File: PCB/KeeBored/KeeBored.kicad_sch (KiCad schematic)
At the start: 114 parts, among them SW1 SW_Push, SW10 SW_Push, SW100 SW_Push, SW101 SW_Push, SW102 SW_Push, SW103 SW_Push, SW104 SW_Push, SW105 SW_Push, SW106 SW_Push, SW107 SW_Push, SW108 SW_Push, SW109 SW_Push, SW11 SW_Push, SW110 SW_Push, SW111 SW_Push, SW112 SW_Push, SW12 SW_Push, SW13 SW_Push, SW14 SW_Push, SW15 SW_Push, SW16 SW_Push, SW17 SW_Push, SW18 SW_Push, SW19 SW_Push, SW2 SW_Push, SW20 SW_Push, SW21 SW_Push, SW22 SW_Push, SW23 SW_Push, SW24 SW_Push, SW25 SW_Push, SW26 SW_Push, SW27 SW_Push, SW28 SW_Push, SW29 SW_Push, SW3 SW_Push, SW30 SW_Push, SW31 SW_Push, SW32 SW_Push, SW33 SW_Push, SW34 SW_Push, SW35 SW_Push, SW36 SW_Push, SW37 SW_Push, SW38 SW_Push, SW39 SW_Push, SW4 SW_Push, SW40 SW_Push, SW41 SW_Push, SW42 SW_Push, SW43 SW_Push, SW44 SW_Push, SW45 SW_Push, SW46 SW_Push, SW47 SW_Push, SW48 SW_Push, SW49 SW_Push, SW5 SW_Push, SW50 SW_Push, SW51 SW_Push, SW52 SW_Push, SW53 SW_Push, SW54 SW_Push, SW55 SW_Push, SW56 SW_Push, SW57 SW_Push, SW58 SW_Push, SW59 SW_Push, SW6 SW_Push, SW60 SW_Push, SW61 SW_Push, SW62 SW_Push, SW63 SW_Push, SW64 SW_Push, SW65 SW_Push, SW66 SW_Push, SW67 SW_Push, SW68 SW_Push, SW69 SW_Push, SW7 SW_Push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

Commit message: Create Key Matrix
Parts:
- removed SW110, SW111, SW112, SW12, SW83, SW97, SW98: SW_Push, symbol Switch:SW_Push
- added D10, D100, D101, D102, D103, D104, D105, D106, D107, D108, D109, D11, D12, D13, D14, D15, D16, D17, D18, D19, D2, D20, D21, D22, D23, D24, D25, D26, D27, D28, D29, D3, D30, D31, D32, D33, D34, D35, D36, D37, D38, D39, D4, D40, D41, D42, D43, D44, D45, D46, D47, D48, D49, D5, D50, D51, D52, D53, D54, D55, D56, D57, D58, D59, D6, D60, D61, D62, D63, D64, D65, D66, D67, D68, D69, D7, D70, D71, D72, D73, D74, D75, D76, D77, D78, D79, D8, D80, D81, D82, D84, D85, D86, D87, D88, D89, D9, D90, D91, D92, D93, D94, D95, D96, D99: 1N4148, Diode_THT:D_DO-35_SOD27_P7.62mm_Horizontal, symbol Diode:1N4148
- added J1: OLED, symbol Connector:Conn_01x04_Pin
- added SW83: RotaryEncoder_Switch, symbol Device:RotaryEncoder_Switch
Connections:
- net C11: now also SW83.S1
- net C4: now also A1.29 (GPIO22); no longer A1.6 (GPIO4)
- net C5: now also A1.31 (GPIO26_ADC0); no longer A1.7 (GPIO5)
- net GND: now also SW83.C
- net R0: now also D1.1 (K), D10.1 (K), D11.1 (K), D12.1 (K), D13.1 (K), D14.1 (K), D2.1 (K), D3.1 (K), D4.1 (K), D5.1 (K), D6.1 (K), D7.1 (K), D8.1 (K), D9.1 (K)
- net R1: now also D15.1 (K), D16.1 (K), D17.1 (K), D18.1 (K), D19.1 (K), D20.1 (K), D21.1 (K), D22.1 (K), D23.1 (K), D24.1 (K), D25.1 (K), D26.1 (K), D27.1 (K), D28.1 (K)
- net R2: now also D29.1 (K), D30.1 (K), D31.1 (K), D32.1 (K), D33.1 (K), D34.1 (K), D35.1 (K), D36.1 (K), D37.1 (K), D38.1 (K), D39.1 (K), D40.1 (K), D41.1 (K), D42.1 (K)
- net R3: now also D43.1 (K), D44.1 (K), D45.1 (K), D46.1 (K), D47.1 (K), D48.1 (K), D49.1 (K), D50.1 (K), D51.1 (K), D52.1 (K), D53.1 (K), D54.1 (K), D55.1 (K), D56.1 (K)
- net R4: now also D57.1 (K), D58.1 (K), D59.1 (K), D60.1 (K), D61.1 (K), D62.1 (K), D63.1 (K), D64.1 (K), D65.1 (K), D66.1 (K), D67.1 (K), D68.1 (K), D69.1 (K), D70.1 (K)
- net R5: now also D71.1 (K), D72.1 (K), D73.1 (K), D74.1 (K), D75.1 (K), D76.1 (K), D77.1 (K), D78.1 (K), D79.1 (K), D80.1 (K), D81.1 (K), D82.1 (K), D84.1 (K)
- net R6: now also D85.1 (K), D86.1 (K), D87.1 (K), D88.1 (K), D89.1 (K), D90.1 (K), D91.1 (K), D92.1 (K), D93.1 (K), D94.1 (K), D95.1 (K), D96.1 (K)
- net R7: now also D100.1 (K), D101.1 (K), D102.1 (K), D103.1 (K), D104.1 (K), D105.1 (K), D106.1 (K), D107.1 (K), D108.1 (K), D109.1 (K), D99.1 (K)
- net at SW85.2: now also D85.2 (A); no longer D1.2 (A)
- net at SW8.2: now also D8.2 (A)
- net at SW84.2: now also D84.2 (A)
- net at SW55.2: now also D55.2 (A)
- net at SW51.2: now also D51.2 (A)
- net at SW102.2: now also D102.2 (A)
- net at SW29.2: now also D29.2 (A)
- net at SW92.2: now also D92.2 (A)
- net at SW33.2: now also D33.2 (A)
- net at SW101.2: now also D101.2 (A)
- net at SW65.2: now also D65.2 (A)
- net at SW43.2: now also D43.2 (A)
- net at SW67.2: now also D67.2 (A)
- net at SW28.2: now also D28.2 (A)
- net at SW90.2: now also D90.2 (A)
- net at SW66.2: now also D66.2 (A)
- net at SW57.2: now also D57.2 (A)
- net at SW104.2: now also D104.2 (A)
- net at SW39.2: now also D39.2 (A)
- net at SW62.2: now also D62.2 (A)
- net at SW108.2: now also D108.2 (A)
- net at SW73.2: now also D73.2 (A)
- net at SW70.2: now also D70.2 (A)
- net at SW46.2: now also D46.2 (A)
- net at SW54.2: now also D54.2 (A)
- net at SW48.2: now also D48.2 (A)
- net at SW80.2: now also D80.2 (A)
- net at SW10.2: now also D10.2 (A)
- net at SW3.2: now also D3.2 (A)
- net at SW82.2: now also D82.2 (A)
- net at SW30.2: now also D30.2 (A)
- net at SW13.2: now also D13.2 (A)
- net at SW109.2: now also D109.2 (A)
- net EC11B: now reaches A1.32 (GPIO27_ADC1)
- net EC11B: now also SW83.B
- net EC11A: now reaches A1.34 (GPIO28_ADC2)
- net EC11A: now also SW83.A
- net at SW59.2: now also D59.2 (A)
- net at SW56.2: now also D56.2 (A)
- net at SW17.2: now also D17.2 (A)
- net at SW64.2: now also D64.2 (A)
- net at SW4.2: now also D4.2 (A)
- net at SW11.2: now also D11.2 (A)
- net at SW74.2: now also D74.2 (A)
- net at SW35.2: now also D35.2 (A)
- net at SW2.2: now also D2.2 (A)
- net at SW60.2: now also D60.2 (A)
- net at SW76.2: now also D76.2 (A)
- net at SW47.2: now also D47.2 (A)
- net at SW106.2: now also D106.2 (A)
- net at SW23.2: now also D23.2 (A)
- net at SW86.2: now also D86.2 (A)
- net at SW6.2: now also D6.2 (A)
- net at SW71.2: now also D71.2 (A)
- net at SW22.2: now also D22.2 (A)
- net at SW27.2: now also D27.2 (A)
- net at SW25.2: now also D25.2 (A)
- net at SW58.2: now also D58.2 (A)
- net at SW42.2: now also D42.2 (A)
- net at SW14.2: now also D14.2 (A)
- net at SW37.2: now also D37.2 (A)
- net at SW81.2: now also D81.2 (A)
- net at SW61.2: now also D61.2 (A)
- net at SW103.2: now also D103.2 (A)
- net at SW16.2: now also D16.2 (A)
- net at SW100.2: now also D100.2 (A)
- net at SW15.2: now also D15.2 (A)
- net at SW21.2: now also D21.2 (A)
- net at SW75.2: now also D75.2 (A)
- net at SW105.2: now also D105.2 (A)
- net at SW68.2: now also D68.2 (A)
- net at SW63.2: now also D63.2 (A)
- net at SW31.2: now also D31.2 (A)
- net at SW20.2: now also D20.2 (A)
- net at SW49.2: now also D49.2 (A)
- net at SW5.2: now also D5.2 (A)
- net at SW19.2: now also D19.2 (A)
- net at SW34.2: now also D34.2 (A)
- net at SW93.2: now also D93.2 (A)
- net at SW88.2: now also D88.2 (A)
- net at SW44.2: now also D44.2 (A)
- net at SW91.2: now also D91.2 (A)
- net at SW94.2: now also D94.2 (A)
- net at SW45.2: now also D45.2 (A)
- net at SW107.2: now also D107.2 (A)
- net at SW89.2: now also D89.2 (A)
- net at SW36.2: now also D36.2 (A)
- net at SW99.2: now also D99.2 (A)
- net at SW24.2: now also D24.2 (A)
- net at SW41.2: now also D41.2 (A)
- net at SW32.2: now also D32.2 (A)
- net at SW96.2: now also D96.2 (A)
- net at SW69.2: now also D69.2 (A)
- net at SW95.2: now also D95.2 (A)
- net at SW79.2: now also D79.2 (A)
- net at SW40.2: now also D40.2 (A)
- net at SW38.2: now also D38.2 (A)
- net at SW78.2: now also D78.2 (A)
- net at SW18.2: now also D18.2 (A)
- net at SW77.2: now also D77.2 (A)
- net at SW26.2: now also D26.2 (A)
- net at SW87.2: now also D87.2 (A)
- net at SW50.2: now also D50.2 (A)
- net at SW52.2: now also D52.2 (A)
- net at SW72.2: now also D72.2 (A)
- net at SW9.2: now also D9.2 (A)
- net at SW53.2: now also D53.2 (A)
- net at SW7.2: now also D7.2 (A)
- net at SW1.2: now also D1.2 (A)
- new net EC11SWB: D12.2 (A), SW83.S2
- new net OLED_SCL: A1.7 (GPIO5)
- new net OLED_SDA: A1.6 (GPIO4)
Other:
- moved on the sheet: A1, SW1, SW10, SW11, SW13, SW14, SW2, SW3, SW4, SW5, SW6, SW7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

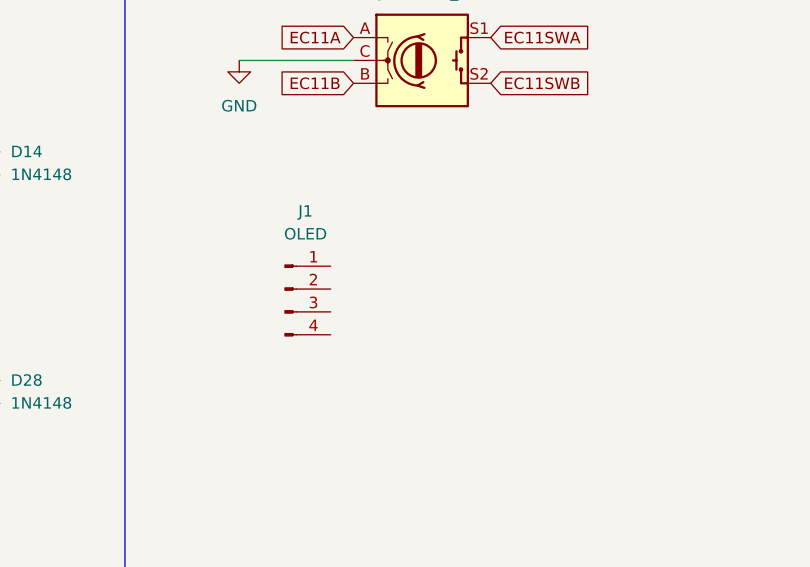
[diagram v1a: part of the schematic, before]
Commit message: Update Schematic (Add Rotary encoder, remove extra switches)
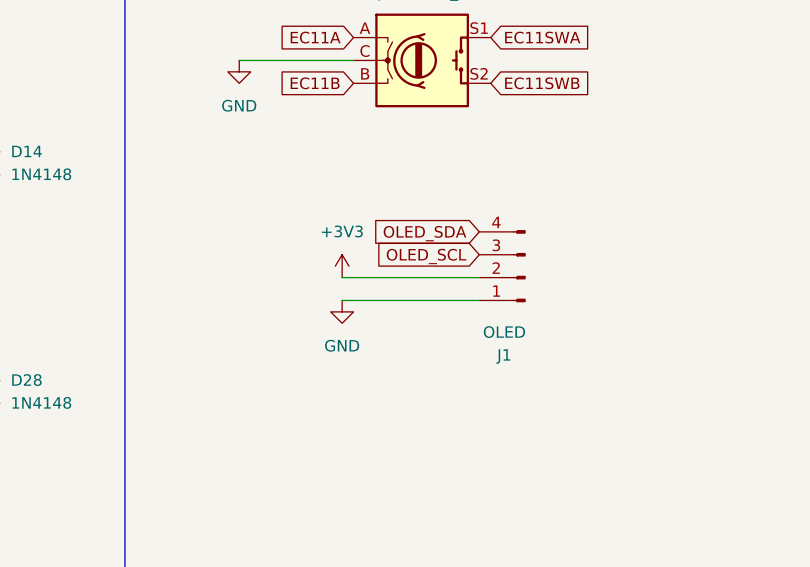
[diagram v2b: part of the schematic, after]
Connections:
- net +3V3: now also J1.2 (Pin_2)
- net GND: now also J1.1 (Pin_1)
- net OLED_SCL: now also J1.3 (Pin_3)
- net OLED_SDA: now also J1.4 (Pin_4)
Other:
- moved on the sheet: J1
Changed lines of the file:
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@@
 	(wire
 		(pts
+			(xy 265.43 54.61) (xy 280.67 54.61)
+		)
+		(stroke
+			(width 0)
+			(type default)
+		)
+	)
+	(wire
+		(pts
 			(xy 99.06 45.72) (xy 99.06 50.8)
 		)
@@
 	(wire
 		(pts
+			(xy 265.43 57.15) (xy 280.67 57.15)
+		)
+		(stroke
+			(width 0)
+			(type default)
+		)
+	)
+	(wire
+		(pts
 			(xy 149.86 45.72) (xy 149.86 50.8)
 		)
@@
 		)
 	)
+	(global_label "OLED_SCL"
+		(shape input)
+		(at 280.67 52.07 180)
+		(fields_autoplaced yes)
+		(effects
+			(font
+				(size 1.27 1.27)
+			)
+			(justify right)
+		)
+		(property "Intersheetrefs" "${INTERSHEET_REFS}"
+			(at 269.0862 52.07 0)
+			(hide yes)
+			(show_name no)
+			(do_not_autoplace no)
+			(effects
+				(font
+					(size 1.27 1.27)
+				)
+				(justify right)
+			)
+		)
+	)
 	(global_label "C9"
 		(shape input)
@@
 		)
 	)
+	(global_label "OLED_SDA"
+		(shape input)
+		(at 280.67 49.53 180)
+		(fields_autoplaced yes)
+		(effects
+			(font
+				(size 1.27 1.27)
+			)
+			(justify right)
+		)
+		(property "Intersheetrefs" "${INTERSHEET_REFS}"
+			(at 269.0257 49.53 0)
+			(hide yes)
+			(show_name no)
+			(do_not_autoplace no)
+			(effects
+				(font
+					(size 1.27 1.27)
+				)
+				(justify right)
+			)
+		)
+	)
 	(global_label "R6"
 		(shape input)
@@
 	)
 	(symbol
+		(lib_id "power:+3V3")
+		(at 265.43 54.61 0)
+		(unit 1)
+		(body_style 1)
+		(exclude_from_sim no)
+		(in_bom yes)
+		(on_board yes)
+		(in_pos_files yes)
+		(dnp no)
+		(fields_autoplaced yes)
+		(property "Reference" "#PWR04"
+			(at 265.43 58.42 0)
+			(hide yes)
+			(show_name no)
+			(do_not_autoplace no)
+			(effects
+				(font
+					(size 1.27 1.27)
+				)
+			)
+		)
+		(property "Value" "+3V3"
+			(at 265.43 49.53 0)
+			(show_name no)
+			(do_not_autoplace no)
+			(effects
+				(font
+					(size 1.27 1.27)
+				)
+			)
+		)
+		(property "Footprint" ""
+			(at 265.43 54.61 0)
+			(hide yes)
+			(show_name no)
+			(do_not_autoplace no)
+			(effects
+				(font
+					(size 1.27 1.27)
+				)
+			)
+		)
+		(property "Datasheet" ""
+			(at 265.43 54.61 0)
+			(hide yes)
+			(show_name no)
+			(do_not_autoplace no)
+			(effects
+				(font
+					(size 1.27 1.27)
+				)
+			)
+		)
+		(property "Description" "Power symbol creates a global label with name \"+3V3\""
+			(at 265.43 54.61 0)
+			(hide yes)
+			(show_name no)
+			(do_not_autoplace no)
+			(effects
+				(font
+					(size 1.27 1.27)
+				)
+			)
+		)
+		(pin "1"
+		)
+		(instances
+			(project "KeeBored"
+				(path "/9bc0cb03-a3e5-4670-9f26-09984cc850ad"
+					(reference "#PWR04")
+					(unit 1)
+				)
+			)
+		)
+	)
+	(symbol
 		(lib_id "Switch:SW_Push")
 		(at 132.08 139.7 0)
@@
 	(symbol
 		(lib_id "Connector:Conn_01x04_Pin")
-		(at 259.08 55.88 0)
+		(at 285.75 54.61 180)
 		(unit 1)
 		(body_style 1)
@@
 		(dnp no)
 		(property "Reference" "J1"
-			(at 261.366 47.244 0)
+			(at 283.464 63.246 0)
 			(show_name no)
 			(do_not_autoplace no)
@@
 		)
 		(property "Value" "OLED"
-			(at 261.366 49.784 0)
+			(at 283.464 60.706 0)
 			(show_name no)
 			(do_not_autoplace no)
@@
 		)
 		(property "Footprint" ""
-			(at 259.08 55.88 0)
+			(at 285.75 54.61 0)
 			(hide yes)
 			(show_name no)
@@
 		)
 		(property "Datasheet" ""
-			(at 259.08 55.88 0)
+			(at 285.75 54.61 0)
 			(hide yes)
 			(show_name no)
@@
 		)
 		(property "Description" "Generic connector, single row, 01x04, script generated"
-			(at 259.08 55.88 0)
+			(at 285.75 54.61 0)
 			(hide yes)
 			(show_name no)
@@
 					(unit 1)
 				)
+			)
+		)
+	)
+	(symbol
+		(lib_id "power:GND")
+		(at 265.43 57.15 0)
+		(unit 1)
+		(body_style 1)
+		(exclude_from_sim no)
+		(in_bom yes)
+		(on_board yes)
+		(in_pos_files yes)
+		(dnp no)
+		(fields_autoplaced yes)
+		(property "Reference" "#PWR05"
+			(at 265.43 63.5 0)
+			(hide yes)
+			(show_name no)
+			(do_not_autoplace no)
+			(effects
+				(font
+					(size 1.27 1.27)
+				)
+			)
+		)
+		(property "Value" "GND"
+			(at 265.43 62.23 0)
+			(show_name no)
+			(do_not_autoplace no)
+			(effects
+				(font
+					(size 1.27 1.27)
+				)
+			)
+		)
+		(property "Footprint" ""
+			(at 265.43 57.15 0)
+			(hide yes)
+			(show_name no)
+			(do_not_autoplace no)
+			(effects
+				(font
+					(size 1.27 1.27)
+				)
+			)
+		)
+		(property "Datasheet" ""
+			(at 265.43 57.15 0)
+			(hide yes)
+			(show_name no)
+			(do_not_autoplace no)
+			(effects
+				(font
+					(size 1.27 1.27)
+				)
+			)
+		)
+		(property "Description" "Power symbol creates a global label with name \"GND\" , ground"
+			(at 265.43 57.15 0)
+			(hide yes)
+			(show_name no)
+			(do_not_autoplace no)
+			(effects
+				(font
+					(size 1.27 1.27)
+				)
+			)
+		)
+		(pin "1"
+		)
+		(instances
+			(project "KeeBored"
+				(path "/9bc0cb03-a3e5-4670-9f26-09984cc850ad"
+					(reference "#PWR05")
+					(unit 1)
+				)
